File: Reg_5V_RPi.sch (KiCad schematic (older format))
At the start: 12 parts, among them U20 TPS54340

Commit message: lots of changes: regulator layout improved bom minimized inner top layer completely gnd UB single pole pullups for use without pi swiched to new kicad version and fp lib motor and servo netanmes fixed added input filtering
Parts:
- added C20, C21: 10µ, Capacitor_SMD:C_0603_1608Metric, symbol Device:C_Small
- C22: renamed from C20; value 10µ -> 100n; footprint Capacitors_SMD:C_0603 -> Capacitor_SMD:C_0603_1608Metric
- C23: renamed from C21; footprint Capacitors_SMD:C_0603 -> Capacitor_SMD:C_0603_1608Metric
- C24: renamed from C22; footprint Capacitors_SMD:C_0603 -> Capacitor_SMD:C_0603_1608Metric
- C25: renamed from C23; footprint Capacitors_SMD:C_0603 -> Capacitor_SMD:C_0603_1608Metric
- C26: renamed from C24; value 47µ -> 100µ; footprint Capacitors_SMD:C_1206 -> Capacitor_SMD:C_1206_3216Metric
- R21, R22: footprint Resistors_SMD:R_0603 -> Resistor_SMD:R_0603_1608Metric
- R23: value 43k -> 180k; footprint Resistors_SMD:R_0603 -> Resistor_SMD:R_0603_1608Metric
- R24: value 8k2 -> 34k; footprint Resistors_SMD:R_0603 -> Resistor_SMD:R_0603_1608Metric
- U20: footprint hedgehog_footprints:HSOP-8 -> Package_SO:HSOP-8-1EP_3.9x4.9mm_P1.27mm_EP2.41x3.1mm_ThermalVias
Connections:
- net GND: now also C20.2, C21.2
- net VIN: now also C20.1, C21.1
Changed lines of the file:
@@
 EESchema Schematic File Version 4
 LIBS:Hedgehog-cache
-EELAYER 26 0
+EELAYER 29 0
 EELAYER END
 $Descr A4 11693 8268
 encoding utf-8
 Sheet 3 5
-Title ""
+Title "Hedgehog"
 Date ""
-Rev ""
+Rev "0.4"
 Comp ""
 Comment1 ""
@@
 Comment4 ""
 $EndDescr
-Text HLabel 4100 3325 0    60   Input ~ 0
+Text HLabel 3525 3325 0    60   Input ~ 0
 VIN
 Text HLabel 5025 3525 0    60   Input ~ 0
@@
 F 0 "U20" H 5675 4075 60  0000 C CNN
 F 1 "TPS54340" H 5675 3175 60  0000 C CNN
-F 2 "hedgehog_footprints:HSOP-8" H 5325 2825 60  0001 C CNN
+F 2 "Package_SO:HSOP-8-1EP_3.9x4.9mm_P1.27mm_EP2.41x3.1mm_ThermalVias" H 5325 2825 60  0001 C CNN
 F 3 "" H 5325 2825 60  0001 C CNN
 	1    5675 3625
@@
 $EndComp
 $Comp
-L Device:C_Small C20
+L Device:C_Small C22
 U 1 1 590647C4
 P 4250 3800
-F 0 "C20" H 4025 3825 50  0000 L CNN
-F 1 "10µ" H 4025 3750 50  0000 L CNN
-F 2 "Capacitors_SMD:C_0603" H 4250 3800 50  0001 C CNN
+F 0 "C22" H 4100 3875 50  0000 L CNN
+F 1 "100n" H 4050 3750 50  0000 L CNN
+F 2 "Capacitor_SMD:C_0603_1608Metric" H 4250 3800 50  0001 C CNN
 F 3 "" H 4250 3800 50  0001 C CNN
 	1    4250 3800
@@
 $EndComp
 $Comp
-L Device:C_Small C21
+L Device:C_Small C23
 U 1 1 59064874
 P 4625 4075
-F 0 "C21" H 4400 4100 50  0000 L CNN
+F 0 "C23" H 4400 4100 50  0000 L CNN
 F 1 "2n4" H 4400 4025 50  0000 L CNN
-F 2 "Capacitors_SMD:C_0603" H 4625 4075 50  0001 C CNN
+F 2 "Capacitor_SMD:C_0603_1608Metric" H 4625 4075 50  0001 C CNN
 F 3 "" H 4625 4075 50  0001 C CNN
 	1    4625 4075
@@
 $EndComp
 $Comp
-L Device:C_Small C22
+L Device:C_Small C24
 U 1 1 590648E6
 P 4800 3925
-F 0 "C22" H 4892 3971 50  0000 L CNN
+F 0 "C24" H 4892 3971 50  0000 L CNN
 F 1 "22p" H 4892 3880 50  0000 L CNN
-F 2 "Capacitors_SMD:C_0603" H 4800 3925 50  0001 C CNN
+F 2 "Capacitor_SMD:C_0603_1608Metric" H 4800 3925 50  0001 C CNN
 F 3 "" H 4800 3925 50  0001 C CNN
 	1    4800 3925
@@
 $EndComp
 $Comp
-L Device:C_Small C23
+L Device:C_Small C25
 U 1 1 59064924
 P 6325 3325
-F 0 "C23" V 6125 3325 50  0000 C CNN
+F 0 "C25" V 6125 3325 50  0000 C CNN
 F 1 "100n" V 6200 3325 50  0000 C CNN
-F 2 "Capacitors_SMD:C_0603" H 6325 3325 50  0001 C CNN
+F 2 "Capacitor_SMD:C_0603_1608Metric" H 6325 3325 50  0001 C CNN
 F 3 "" H 6325 3325 50  0001 C CNN
 	1    6325 3325
@@
 $EndComp
 $Comp
-L Device:C_Small C24
+L Device:C_Small C26
 U 1 1 59064990
 P 7325 3825
-F 0 "C24" H 7417 3871 50  0000 L CNN
-F 1 "47µ" H 7417 3780 50  0000 L CNN
-F 2 "Capacitors_SMD:C_1206" H 7325 3825 50  0001 C CNN
+F 0 "C26" H 7417 3871 50  0000 L CNN
+F 1 "100µ" H 7417 3780 50  0000 L CNN
+F 2 "Capacitor_SMD:C_1206_3216Metric" H 7325 3825 50  0001 C CNN
 F 3 "" H 7325 3825 50  0001 C CNN
 	1    7325 3825
@@
 F 0 "R21" H 4425 3900 50  0000 L CNN
 F 1 "12k" H 4425 3825 50  0000 L CNN
-F 2 "Resistors_SMD:R_0603" H 4625 3850 50  0001 C CNN
+F 2 "Resistor_SMD:R_0603_1608Metric" H 4625 3850 50  0001 C CNN
 F 3 "" H 4625 3850 50  0001 C CNN
 	1    4625 3850
@@
 F 0 "R22" H 5159 4121 50  0000 L CNN
 F 1 "82k" H 5159 4030 50  0000 L CNN
-F 2 "Resistors_SMD:R_0603" H 5100 4075 50  0001 C CNN
+F 2 "Resistor_SMD:R_0603_1608Metric" H 5100 4075 50  0001 C CNN
 F 3 "" H 5100 4075 50  0001 C CNN
 	1    5100 4075
@@
 P 6975 3675
 F 0 "R23" H 7034 3721 50  0000 L CNN
-F 1 "43k" H 7034 3630 50  0000 L CNN
-F 2 "Resistors_SMD:R_0603" H 6975 3675 50  0001 C CNN
+F 1 "180k" H 7034 3630 50  0000 L CNN
+F 2 "Resistor_SMD:R_0603_1608Metric" H 6975 3675 50  0001 C CNN
 F 3 "" H 6975 3675 50  0001 C CNN
 	1    6975 3675
@@
 P 6975 3975
 F 0 "R24" H 7034 4021 50  0000 L CNN
-F 1 "8k2" H 7034 3930 50  0000 L CNN
-F 2 "Resistors_SMD:R_0603" H 6975 3975 50  0001 C CNN
+F 1 "34k" H 7034 3930 50  0000 L CNN
+F 2 "Resistor_SMD:R_0603_1608Metric" H 6975 3975 50  0001 C CNN
 F 3 "" H 6975 3975 50  0001 C CNN
 	1    6975 3975
@@
 	5100 3925 5100 3975
 Wire Wire Line
-	4625 3725 5175 3725
+	4625 3725 4800 3725
 Wire Wire Line
 	4625 3725 4625 3750
@@
 	5025 3525 5175 3525
 Wire Wire Line
-	4100 3325 5175 3325
+	3525 3325 3800 3325
 Wire Wire Line
 	4250 3325 4250 3700
@@
 	6175 3325 6225 3325
 Wire Wire Line
-	6425 3325 6725 3325
+	6425 3325 6450 3325
 Wire Wire Line
 	6450 3325 6450 3475
@@
 Connection ~ 6575 3325
 Wire Wire Line
-	6925 3325 7400 3325
+	6925 3325 6975 3325
 Wire Wire Line
 	6975 3325 6975 3575
@@
 Connection ~ 7325 3325
 Wire Wire Line
-	6975 3775 6975 3875
+	6975 3775 6975 3825
 $Comp
 L power:GND #PWR07
@@
 Connection ~ 6975 3825
 Wire Wire Line
-	4250 4250 7325 4250
+	4250 4250 4625 4250
 Wire Wire Line
 	4250 4250 4250 3900
@@
 	6175 3825 6250 3825
 Wire Wire Line
-	6250 3825 6250 4250
+	6250 3825 6250 3925
 Connection ~ 6250 4250
 Wire Wire Line
@@
 Text Notes 10575 6525 0    118  ~ 0
 Ref: 2x
+Wire Wire Line
+	4800 3725 5175 3725
+Wire Wire Line
+	4250 3325 5175 3325
+Wire Wire Line
+	6450 3325 6575 3325
+Wire Wire Line
+	6575 3325 6725 3325
+Wire Wire Line
+	6975 3325 7325 3325
+Wire Wire Line
+	7325 3325 7400 3325
+Wire Wire Line
+	6975 3825 6975 3875
+Wire Wire Line
+	4625 4250 4800 4250
+Wire Wire Line
+	4800 4250 5100 4250
+Wire Wire Line
+	5100 4250 5675 4250
+Wire Wire Line
+	5675 4250 6250 4250
+Wire Wire Line
+	6975 4250 7325 4250
+Wire Wire Line
+	6250 4250 6975 4250
+Wire Wire Line
+	6250 3925 6250 4250
+$Comp
+L Device:C_Small C21
+U 1 1 5CECD2BB
+P 4000 3800
+F 0 "C21" H 3850 3875 50  0000 L CNN
+F 1 "10µ" H 3850 3750 50  0000 L CNN
+F 2 "Capacitor_SMD:C_0603_1608Metric" H 4000 3800 50  0001 C CNN
+F 3 "" H 4000 3800 50  0001 C CNN
+	1    4000 3800
+	1    0    0    -1
+$EndComp
+$Comp
+L Device:C_Small C20
+U 1 1 5CECD4E2
+P 3800 3800
+F 0 "C20" H 3650 3875 50  0000 L CNN
+F 1 "10µ" H 3650 3750 50  0000 L CNN
+F 2 "Capacitor_SMD:C_0603_1608Metric" H 3800 3800 50  0001 C CNN
+F 3 "" H 3800 3800 50  0001 C CNN
+	1    3800 3800
+	1    0    0    -1
+$EndComp
+Wire Wire Line
+	4000 3700 4000 3325
+Connection ~ 4000 3325
+Wire Wire Line
+	4000 3325 4250 3325
+Wire Wire Line
+	3800 3700 3800 3325
+Connection ~ 3800 3325
+Wire Wire Line
+	3800 3325 4000 3325
+Wire Wire Line
+	4000 3900 4000 4250
+Wire Wire Line
+	4000 4250 4250 4250
+Connection ~ 4250 4250
+Wire Wire Line
+	3800 3900 3800 4250
+Wire Wire Line
+	3800 4250 4000 4250
+Connection ~ 4000 4250
 $EndSCHEMATC

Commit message: changed 3V3 regulator to different IC D20 smaller added 5V RPi Reg EN pulldown
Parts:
- added R21: 1k2, Resistor_SMD:R_0603_1608Metric, symbol Device:R_Small
- D20: value D -> VSSAF5L45; footprint hedgehog_footprints:PDS760-13 -> hedgehog_footprints:D_DO-221AC
- U20: footprint Package_SO:HSOP-8-1EP_3.9x4.9mm_P1.27mm_EP2.41x3.1mm_ThermalVias -> hedgehog_footprints:HSOP-8-1EP_3.9x4.9mm_P1.27mm_EP2.41x3.1mm_ThermalVias
- renumbered R21 to R22, R22 to R23, R23 to R24, R24 to R25
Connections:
- net EN: now also R21.1
- net GND: now also R21.2
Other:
- moved on the sheet: C20, C21, C22
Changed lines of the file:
@@
 Comment4 ""
 $EndDescr
-Text HLabel 3525 3325 0    60   Input ~ 0
+Text HLabel 3225 3325 0    60   Input ~ 0
 VIN
-Text HLabel 5025 3525 0    60   Input ~ 0
+Text HLabel 4275 3525 0    60   Input ~ 0
 EN
 Text HLabel 7400 3325 2    60   Input ~ 0
@@
 F 0 "U20" H 5675 4075 60  0000 C CNN
 F 1 "TPS54340" H 5675 3175 60  0000 C CNN
-F 2 "Package_SO:HSOP-8-1EP_3.9x4.9mm_P1.27mm_EP2.41x3.1mm_ThermalVias" H 5325 2825 60  0001 C CNN
+F 2 "hedgehog_footprints:HSOP-8-1EP_3.9x4.9mm_P1.27mm_EP2.41x3.1mm_ThermalVias" H 5325 2825 60  0001 C CNN
 F 3 "" H 5325 2825 60  0001 C CNN
 	1    5675 3625
@@
 L Device:C_Small C22
 U 1 1 590647C4
-P 4250 3800
-F 0 "C22" H 4100 3875 50  0000 L CNN
-F 1 "100n" H 4050 3750 50  0000 L CNN
-F 2 "Capacitor_SMD:C_0603_1608Metric" H 4250 3800 50  0001 C CNN
-F 3 "" H 4250 3800 50  0001 C CNN
-	1    4250 3800
+P 3950 3800
+F 0 "C22" H 3800 3875 50  0000 L CNN
+F 1 "100n" H 3750 3750 50  0000 L CNN
+F 2 "Capacitor_SMD:C_0603_1608Metric" H 3950 3800 50  0001 C CNN
+F 3 "" H 3950 3800 50  0001 C CNN
+	1    3950 3800
 	1    0    0    -1
 $EndComp
@@
 $EndComp
 $Comp
-L Device:R_Small R21
+L Device:R_Small R22
 U 1 1 59064A14
 P 4625 3850
-F 0 "R21" H 4425 3900 50  0000 L CNN
+F 0 "R22" H 4425 3900 50  0000 L CNN
 F 1 "12k" H 4425 3825 50  0000 L CNN
 F 2 "Resistor_SMD:R_0603_1608Metric" H 4625 3850 50  0001 C CNN
@@
 $EndComp
 $Comp
-L Device:R_Small R22
+L Device:R_Small R23
 U 1 1 59064AB0
 P 5100 4075
-F 0 "R22" H 5159 4121 50  0000 L CNN
+F 0 "R23" H 5159 4121 50  0000 L CNN
 F 1 "82k" H 5159 4030 50  0000 L CNN
 F 2 "Resistor_SMD:R_0603_1608Metric" H 5100 4075 50  0001 C CNN
@@
 $EndComp
 $Comp
-L Device:R_Small R23
+L Device:R_Small R24
 U 1 1 59064B04
 P 6975 3675
-F 0 "R23" H 7034 3721 50  0000 L CNN
+F 0 "R24" H 7034 3721 50  0000 L CNN
 F 1 "180k" H 7034 3630 50  0000 L CNN
 F 2 "Resistor_SMD:R_0603_1608Metric" H 6975 3675 50  0001 C CNN
@@
 $EndComp
 $Comp
-L Device:R_Small R24
+L Device:R_Small R25
 U 1 1 59064B72
 P 6975 3975
-F 0 "R24" H 7034 4021 50  0000 L CNN
+F 0 "R25" H 7034 4021 50  0000 L CNN
 F 1 "34k" H 7034 3930 50  0000 L CNN
 F 2 "Resistor_SMD:R_0603_1608Metric" H 6975 3975 50  0001 C CNN
@@
 P 6575 3450
 F 0 "D20" V 6529 3518 50  0000 L CNN
-F 1 "D" V 6620 3518 50  0000 L CNN
-F 2 "hedgehog_footprints:PDS760-13" V 6575 3450 50  0001 C CNN
+F 1 "VSSAF5L45" V 6620 3518 50  0000 L CNN
+F 2 "hedgehog_footprints:D_DO-221AC" V 6575 3450 50  0001 C CNN
 F 3 "" V 6575 3450 50  0001 C CNN
 	1    6575 3450
@@
 Connection ~ 4800 3725
 Wire Wire Line
-	5025 3525 5175 3525
-Wire Wire Line
-	3525 3325 3800 3325
-Wire Wire Line
-	4250 3325 4250 3700
-Connection ~ 4250 3325
+	4275 3525 4350 3525
+Wire Wire Line
+	3225 3325 3500 3325
+Wire Wire Line
+	3950 3325 3950 3700
+Connection ~ 3950 3325
 Wire Wire Line
 	6175 3325 6225 3325
@@
 Connection ~ 6975 3825
 Wire Wire Line
-	4250 4250 4625 4250
-Wire Wire Line
-	4250 4250 4250 3900
+	3950 4250 3950 3900
 Wire Wire Line
 	4625 4175 4625 4250
-Connection ~ 4625 4250
 Wire Wire Line
 	4800 4025 4800 4250
@@
 	4800 3725 5175 3725
 Wire Wire Line
-	4250 3325 5175 3325
-Wire Wire Line
 	6450 3325 6575 3325
 Wire Wire Line
@@
 L Device:C_Small C21
 U 1 1 5CECD2BB
-P 4000 3800
-F 0 "C21" H 3850 3875 50  0000 L CNN
-F 1 "10µ" H 3850 3750 50  0000 L CNN
-F 2 "Capacitor_SMD:C_0603_1608Metric" H 4000 3800 50  0001 C CNN
-F 3 "" H 4000 3800 50  0001 C CNN
-	1    4000 3800
+P 3700 3800
+F 0 "C21" H 3550 3875 50  0000 L CNN
+F 1 "10µ" H 3550 3750 50  0000 L CNN
+F 2 "Capacitor_SMD:C_0603_1608Metric" H 3700 3800 50  0001 C CNN
+F 3 "" H 3700 3800 50  0001 C CNN
+	1    3700 3800
 	1    0    0    -1
 $EndComp
@@
 L Device:C_Small C20
 U 1 1 5CECD4E2
-P 3800 3800
-F 0 "C20" H 3650 3875 50  0000 L CNN
-F 1 "10µ" H 3650 3750 50  0000 L CNN
-F 2 "Capacitor_SMD:C_0603_1608Metric" H 3800 3800 50  0001 C CNN
-F 3 "" H 3800 3800 50  0001 C CNN
-	1    3800 3800
-	1    0    0    -1
-$EndComp
-Wire Wire Line
-	4000 3700 4000 3325
-Connection ~ 4000 3325
-Wire Wire Line
-	4000 3325 4250 3325
-Wire Wire Line
-	3800 3700 3800 3325
-Connection ~ 3800 3325
-Wire Wire Line
-	3800 3325 4000 3325
-Wire Wire Line
-	4000 3900 4000 4250
-Wire Wire Line
-	4000 4250 4250 4250
-Connection ~ 4250 4250
-Wire Wire Line
-	3800 3900 3800 4250
-Wire Wire Line
-	3800 4250 4000 4250
-Connection ~ 4000 4250
+P 3500 3800
+F 0 "C20" H 3350 3875 50  0000 L CNN
+F 1 "10µ" H 3350 3750 50  0000 L CNN
+F 2 "Capacitor_SMD:C_0603_1608Metric" H 3500 3800 50  0001 C CNN
+F 3 "" H 3500 3800 50  0001 C CNN
+	1    3500 3800
+	1    0    0    -1
+$EndComp
+Wire Wire Line
+	3700 3700 3700 3325
+Connection ~ 3700 3325
+Wire Wire Line
+	3700 3325 3950 3325
+Wire Wire Line
+	3500 3700 3500 3325
+Connection ~ 3500 3325
+Wire Wire Line
+	3500 3325 3700 3325
+Wire Wire Line
+	3700 3900 3700 4250
+Wire Wire Line
+	3700 4250 3950 4250
+Connection ~ 3950 4250
+Wire Wire Line
+	3500 3900 3500 4250
+Wire Wire Line
+	3500 4250 3700 4250
+Connection ~ 3700 4250
+$Comp
+L Device:R_Small R21
+U 1 1 5BD9CEE1
+P 4350 3850
+F 0 "R21" H 4150 3900 50  0000 L CNN
+F 1 "1k2" H 4150 3825 50  0000 L CNN
+F 2 "Resistor_SMD:R_0603_1608Metric" H 4350 3850 50  0001 C CNN
+F 3 "" H 4350 3850 50  0001 C CNN
+	1    4350 3850
+	1    0    0    -1
+$EndComp
+Wire Wire Line
+	3950 4250 4350 4250
+Connection ~ 4625 4250
+Wire Wire Line
+	3950 3325 5175 3325
+Wire Wire Line
+	4350 3950 4350 4250
+Connection ~ 4350 4250
+Wire Wire Line
+	4350 4250 4625 4250
+Wire Wire Line
+	4350 3750 4350 3525
+Connection ~ 4350 3525
+Wire Wire Line
+	4350 3525 5175 3525
 $EndSCHEMATC

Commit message: Updated documentation and other small changes
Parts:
- R21: value 1k2 -> 1k8
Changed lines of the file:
@@
 P 4350 3850
 F 0 "R21" H 4150 3900 50  0000 L CNN
-F 1 "1k2" H 4150 3825 50  0000 L CNN
+F 1 "1k8" H 4150 3825 50  0000 L CNN
 F 2 "Resistor_SMD:R_0603_1608Metric" H 4350 3850 50  0001 C CNN
 F 3 "" H 4350 3850 50  0001 C CNN

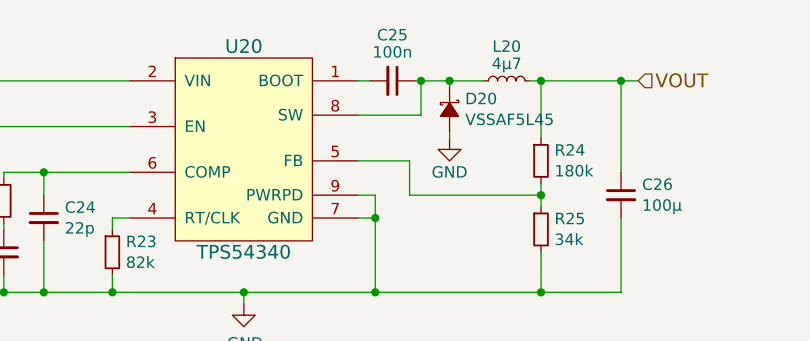
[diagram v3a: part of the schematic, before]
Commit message: changes for first production version v1.0: added bootstrap resistor R26 R54 Pullup 5V MS Zones bigger U10 Pin7 GND silk improvements version changed: silk, sch & pcb pages updated doc files
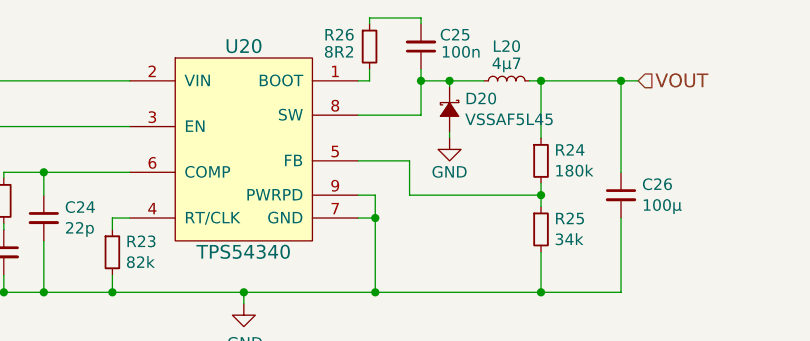
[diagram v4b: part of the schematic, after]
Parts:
- added R26: 8R2, Resistor_SMD:R_0603_1608Metric, symbol Device:R_Small
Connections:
- net at U20.1 (BOOT): now also R26.2; no longer C25.2
- new net: C25.2, R26.1
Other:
- moved on the sheet: C25
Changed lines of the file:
@@
 Sheet 3 5
 Title "Hedgehog"
-Date ""
-Rev "0.4"
+Date "2019-05-12"
+Rev "1.0"
 Comp ""
 Comment1 ""
@@
 L Device:C_Small C25
 U 1 1 59064924
-P 6325 3325
-F 0 "C25" V 6125 3325 50  0000 C CNN
-F 1 "100n" V 6200 3325 50  0000 C CNN
-F 2 "Capacitor_SMD:C_0603_1608Metric" H 6325 3325 50  0001 C CNN
-F 3 "" H 6325 3325 50  0001 C CNN
-	1    6325 3325
-	0    1    1    0
+P 6450 3175
+F 0 "C25" H 6300 3125 50  0000 C CNN
+F 1 "100n" H 6275 3200 50  0000 C CNN
+F 2 "Capacitor_SMD:C_0603_1608Metric" H 6450 3175 50  0001 C CNN
+F 3 "" H 6450 3175 50  0001 C CNN
+	1    6450 3175
+	-1   0    0    1
 $EndComp
 $Comp
@@
 	6175 3325 6225 3325
 Wire Wire Line
-	6425 3325 6450 3325
-Wire Wire Line
 	6450 3325 6450 3475
 Wire Wire Line
@@
 Wire Wire Line
 	6575 3325 6575 3350
-Connection ~ 6450 3325
 Connection ~ 6575 3325
 Wire Wire Line
@@
 Wire Wire Line
 	4350 3525 5175 3525
+$Comp
+L Device:R_Small R26
+U 1 1 5BF09FBC
+P 6225 3175
+F 0 "R26" H 6025 3225 50  0000 L CNN
+F 1 "8R2" H 6025 3150 50  0000 L CNN
+F 2 "Resistor_SMD:R_0603_1608Metric" H 6225 3175 50  0001 C CNN
+F 3 "" H 6225 3175 50  0001 C CNN
+	1    6225 3175
+	1    0    0    -1
+$EndComp
+Wire Wire Line
+	6450 3275 6450 3325
+Connection ~ 6450 3325
+Wire Wire Line
+	6225 3275 6225 3325
+Wire Wire Line
+	6225 3075 6225 3050
+Wire Wire Line
+	6225 3050 6450 3050
+Wire Wire Line
+	6450 3050 6450 3075
 $EndSCHEMATC
